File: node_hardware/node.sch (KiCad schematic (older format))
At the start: 22 parts, among them IC1 bluepill, IC2 Ra-01, IC3 TPS73201, J1 Serial, J2 Sensor1, J3 Sensor2

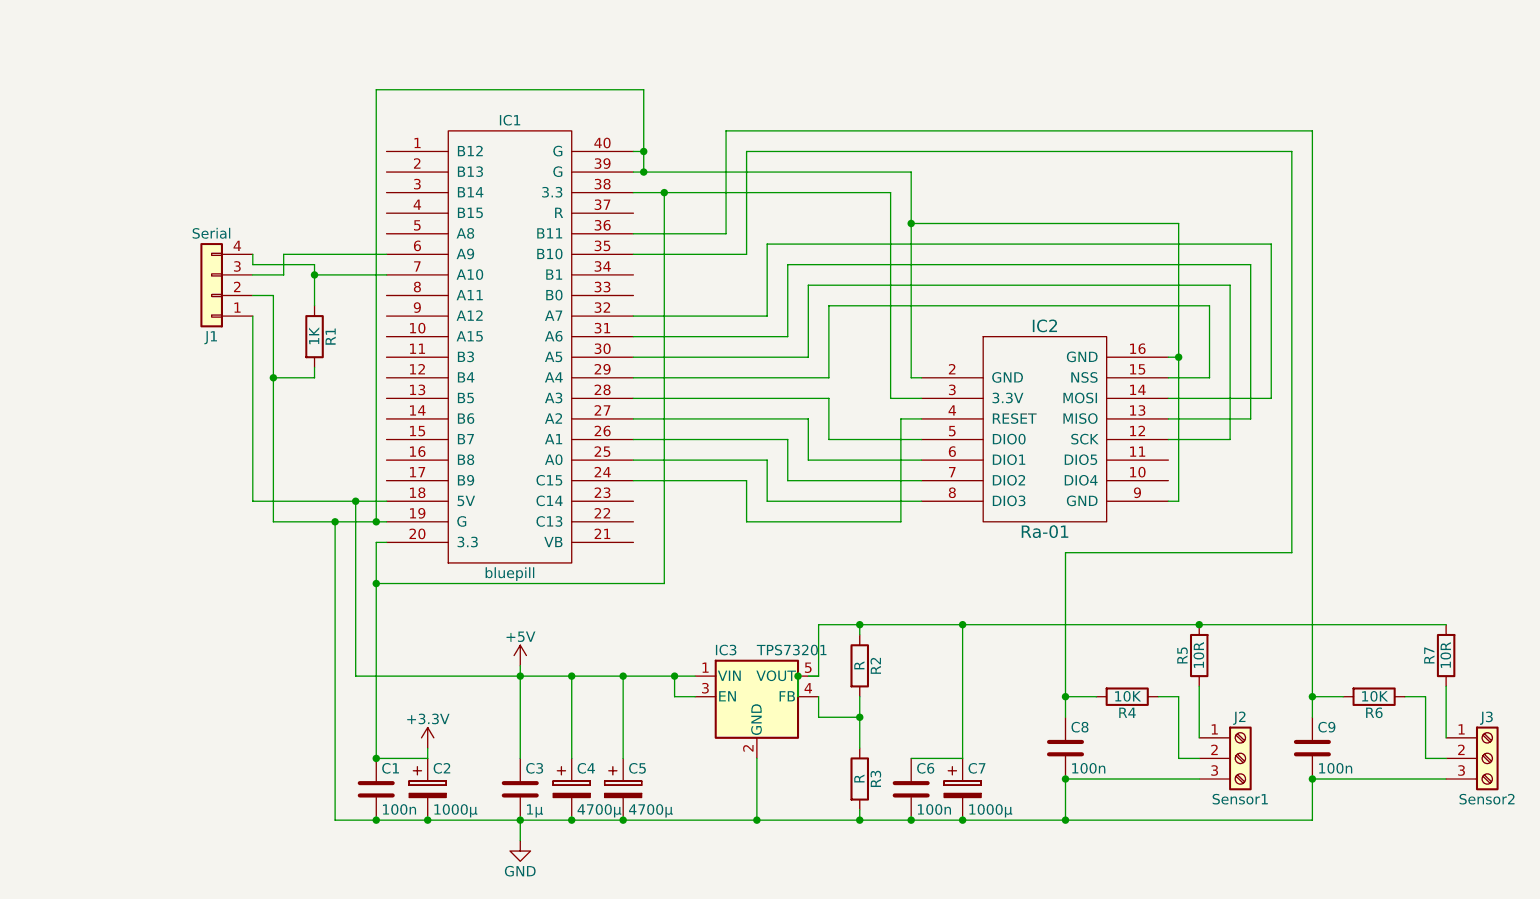
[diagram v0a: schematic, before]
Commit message: Better Layout + added extension headers
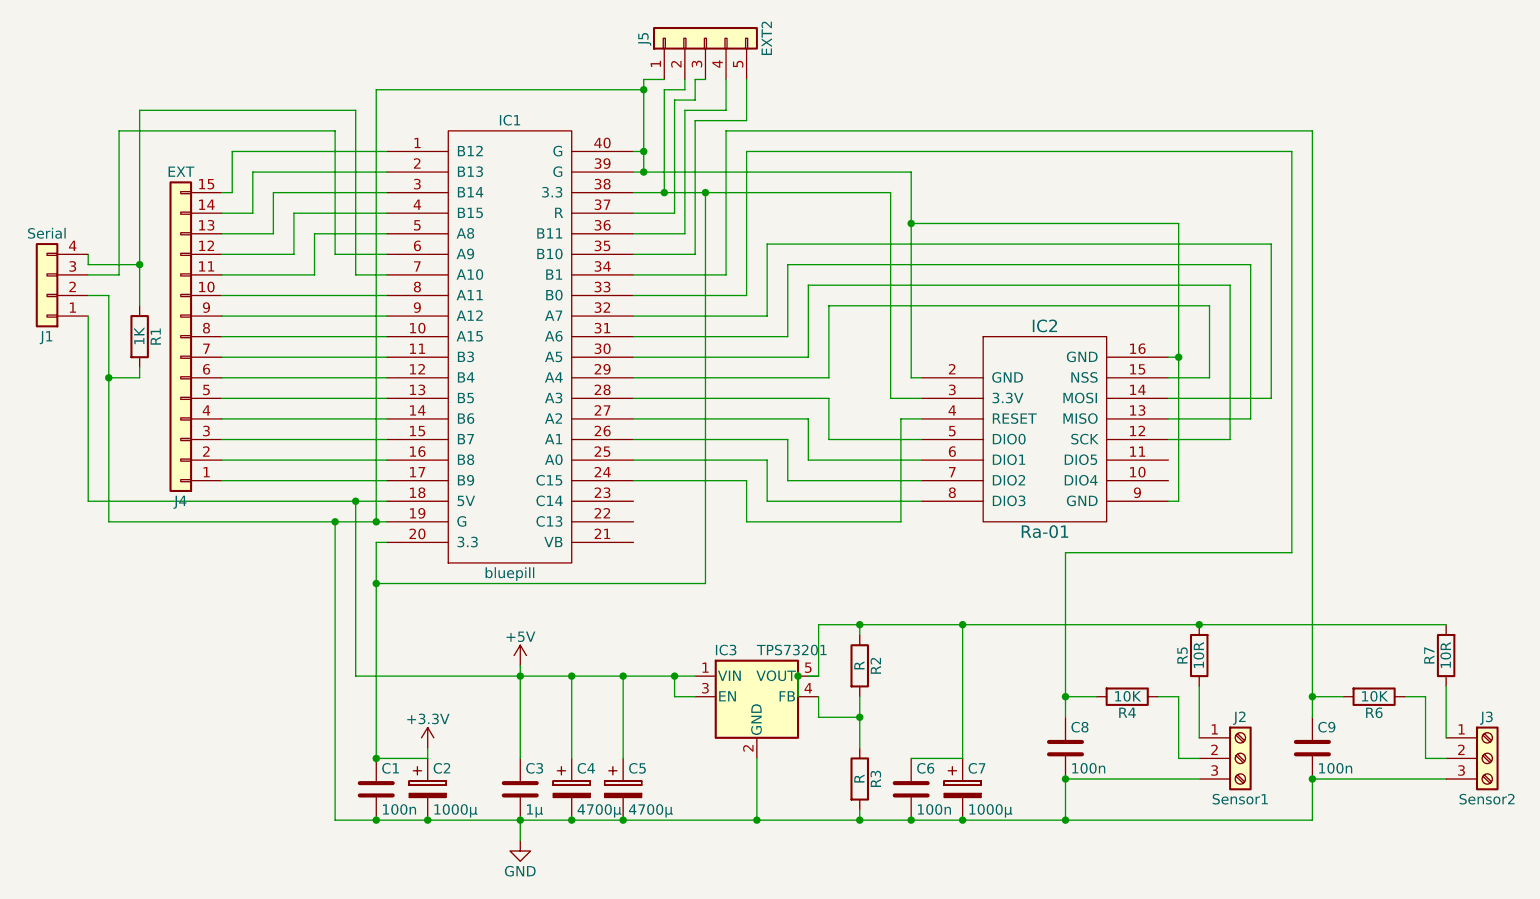
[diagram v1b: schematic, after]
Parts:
- added J4: EXT, Pin_Headers:Pin_Header_Straight_1x15_Pitch2.54mm, symbol Conn_01x15
- added J5: EXT2, Pin_Headers:Pin_Header_Straight_1x05_Pitch2.54mm, symbol Conn_01x05
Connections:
- net +3V3: now also J5.2 (Pin_2)
- net GND: now also J5.1 (Pin_1)
- net at IC1.1 (B12): now also J4.15 (Pin_15)
- net at IC1.10 (A15): now also J4.8 (Pin_8)
- net at IC1.11 (B3): now also J4.7 (Pin_7)
- net at IC1.12 (B4): now also J4.6 (Pin_6)
- net at IC1.13 (B5): now also J4.5 (Pin_5)
- net at IC1.14 (B6): now also J4.4 (Pin_4)
- net at IC1.15 (B7): now also J4.3 (Pin_3)
- net at IC1.16 (B8): now also J4.2 (Pin_2)
- net at IC1.17 (B9): now also J4.1 (Pin_1)
- net at IC1.2 (B13): now also J4.14 (Pin_14)
- net at IC1.3 (B14): now also J4.13 (Pin_13)
- net at IC1.33 (B0): now also C8.1, R4.2
- net at IC1.34 (B1): now also C9.1, R6.2
- net at IC1.37 (R): now also J5.3 (Pin_3)
- net at IC1.4 (B15): now also J4.12 (Pin_12)
- net at IC1.5 (A8): now also J4.11 (Pin_11)
- net at IC1.8 (A11): now also J4.10 (Pin_10)
- net at IC1.9 (A12): now also J4.9 (Pin_9)
- new net: IC1.35 (B10), J5.5 (Pin_5)
- new net: IC1.36 (B11), J5.4 (Pin_4)
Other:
- moved on the sheet: J1, R1
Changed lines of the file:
@@
 L Conn_01x04 J1
 U 1 1 59EA5273
-P 2400 2950
-F 0 "J1" H 2400 3150 50  0000 C CNN
-F 1 "Serial" H 2400 2650 50  0000 C CNN
-F 2 "Pin_Headers:Pin_Header_Straight_1x04_Pitch2.54mm" H 2400 2950 50  0001 C CNN
-F 3 "" H 2400 2950 50  0001 C CNN
-	1    2400 2950
+P 1600 2950
+F 0 "J1" H 1600 3150 50  0000 C CNN
+F 1 "Serial" H 1600 2650 50  0000 C CNN
+F 2 "Pin_Headers:Pin_Header_Straight_1x04_Pitch2.54mm" H 1600 2950 50  0001 C CNN
+F 3 "" H 1600 2950 50  0001 C CNN
+	1    1600 2950
 	-1   0    0    1
 $EndComp
@@
 L R R1
 U 1 1 59EA56C8
-P 2900 3150
-F 0 "R1" V 2980 3150 50  0000 C CNN
-F 1 "1K" V 2900 3150 50  0000 C CNN
-F 2 "Resistors_ThroughHole:R_Axial_DIN0309_L9.0mm_D3.2mm_P12.70mm_Horizontal" V 2830 3150 50  0001 C CNN
-F 3 "" H 2900 3150 50  0001 C CNN
-	1    2900 3150
+P 2050 3150
+F 0 "R1" V 2130 3150 50  0000 C CNN
+F 1 "1K" V 2050 3150 50  0000 C CNN
+F 2 "Resistors_ThroughHole:R_Axial_DIN0309_L9.0mm_D3.2mm_P12.70mm_Horizontal" V 1980 3150 50  0001 C CNN
+F 3 "" H 2050 3150 50  0001 C CNN
+	1    2050 3150
 	1    0    0    -1
 $EndComp
@@
 	5050 5500 5050 5200
 Wire Wire Line
-	5000 2250 5000 2750
-Wire Wire Line
-	5000 2750 4450 2750
+	5000 2250 5000 2950
 Connection ~ 6550 4900
 Wire Wire Line
-	4900 2150 4900 2650
-Wire Wire Line
-	4900 2650 4450 2650
+	4900 2150 4900 2850
 Connection ~ 7750 4900
 Wire Wire Line
@@
 Connection ~ 4400 4800
 Wire Wire Line
-	2700 2950 2700 4050
-Wire Wire Line
-	2700 2950 2600 2950
-Wire Wire Line
-	2600 3050 2600 3950
-Wire Wire Line
-	2900 3300 2900 3350
-Wire Wire Line
-	2900 3350 2700 3350
-Connection ~ 2700 3350
-Wire Wire Line
-	2600 3950 3250 3950
+	1900 2950 1900 4050
+Wire Wire Line
+	1900 2950 1800 2950
+Wire Wire Line
+	1800 3050 1800 3950
+Wire Wire Line
+	2050 3300 2050 3350
+Wire Wire Line
+	2050 3350 1900 3350
+Connection ~ 1900 3350
+Wire Wire Line
+	1800 3950 3250 3950
 Wire Wire Line
 	3100 4800 3100 3950
@@
 Connection ~ 3900 4800
 Wire Wire Line
-	3000 5500 3000 4050
+	3000 4050 3000 5500
 Connection ~ 3000 4050
 Connection ~ 3900 5500
@@
 	3200 4150 3200 5200
 Wire Wire Line
-	2700 4050 3250 4050
+	1900 4050 3250 4050
 Wire Wire Line
 	3200 4150 3250 4150
@@
 	3900 5500 3900 5600
 Wire Wire Line
-	4500 1950 4500 2350
+	4500 1900 4500 2350
 Wire Wire Line
 	4500 2250 4450 2250
@@
 Connection ~ 4500 2250
 Wire Wire Line
-	4600 2450 4600 4350
-Wire Wire Line
-	4600 4350 3200 4350
+	4800 2450 4800 4350
+Wire Wire Line
+	4800 4350 3200 4350
 Connection ~ 3200 4350
-Connection ~ 4600 2450
+Connection ~ 4800 2450
 Wire Wire Line
 	3000 5500 7750 5500
@@
 	6550 4200 7650 4200
 Wire Wire Line
-	3250 2750 2750 2750
-Wire Wire Line
-	2750 2750 2750 2850
-Wire Wire Line
-	2750 2850 2600 2850
-Wire Wire Line
-	2900 3000 2900 2800
-Wire Wire Line
-	2900 2800 2600 2800
-Wire Wire Line
-	2600 2800 2600 2750
-Wire Wire Line
-	3250 2850 2900 2850
-Connection ~ 2900 2850
+	1950 2150 1950 2850
+Wire Wire Line
+	1950 2850 1800 2850
+Wire Wire Line
+	2050 2050 2050 3000
+Wire Wire Line
+	2050 2800 1800 2800
+Wire Wire Line
+	1800 2800 1800 2750
+Wire Wire Line
+	5000 2950 4450 2950
+Wire Wire Line
+	4900 2850 4450 2850
+$Comp
+L Conn_01x15 J4
+U 1 1 59F0A7BB
+P 2250 3150
+F 0 "J4" H 2250 3950 50  0000 C CNN
+F 1 "EXT" H 2250 2350 50  0000 C CNN
+F 2 "Pin_Headers:Pin_Header_Straight_1x15_Pitch2.54mm" H 2250 3150 50  0001 C CNN
+F 3 "" H 2250 3150 50  0001 C CNN
+	1    2250 3150
+	-1   0    0    1
+$EndComp
+Wire Wire Line
+	2450 3850 3250 3850
+Wire Wire Line
+	2450 3750 3250 3750
+Wire Wire Line
+	3250 3650 2450 3650
+Wire Wire Line
+	2450 3550 3250 3550
+Wire Wire Line
+	3250 3450 2450 3450
+Wire Wire Line
+	2450 3350 3250 3350
+Wire Wire Line
+	3250 3250 2450 3250
+Wire Wire Line
+	2450 3150 3250 3150
+Wire Wire Line
+	3250 3050 2450 3050
+Wire Wire Line
+	2450 2950 3250 2950
+Wire Wire Line
+	2450 2450 2500 2450
+Wire Wire Line
+	2500 2450 2500 2250
+Wire Wire Line
+	2500 2250 3250 2250
+Wire Wire Line
+	3250 2350 2600 2350
+Wire Wire Line
+	2600 2350 2600 2550
+Wire Wire Line
+	2600 2550 2450 2550
+Wire Wire Line
+	2450 2650 2700 2650
+Wire Wire Line
+	2700 2650 2700 2450
+Wire Wire Line
+	2700 2450 3250 2450
+Wire Wire Line
+	3250 2550 2800 2550
+Wire Wire Line
+	2800 2550 2800 2750
+Wire Wire Line
+	2800 2750 2450 2750
+Wire Wire Line
+	2450 2850 2900 2850
+Wire Wire Line
+	2900 2850 2900 2650
+Wire Wire Line
+	2900 2650 3250 2650
+Wire Wire Line
+	1950 2150 3000 2150
+Wire Wire Line
+	3000 2150 3000 2750
+Wire Wire Line
+	3000 2750 3250 2750
+Wire Wire Line
+	2050 2050 3100 2050
+Wire Wire Line
+	3100 2050 3100 2850
+Wire Wire Line
+	3100 2850 3250 2850
+Connection ~ 2050 2800
+Wire Wire Line
+	4450 2550 4650 2550
+Wire Wire Line
+	4450 2750 4750 2750
+$Comp
+L Conn_01x05 J5
+U 1 1 59F0D84C
+P 4800 1700
+F 0 "J5" H 4800 2000 50  0000 C CNN
+F 1 "EXT2" H 4800 1400 50  0000 C CNN
+F 2 "Pin_Headers:Pin_Header_Straight_1x05_Pitch2.54mm" H 4800 1700 50  0001 C CNN
+F 3 "" H 4800 1700 50  0001 C CNN
+	1    4800 1700
+	0    -1   -1   0
+$EndComp
+Wire Wire Line
+	4600 1900 4500 1900
+Connection ~ 4500 1950
+Wire Wire Line
+	4700 1900 4700 1950
+Wire Wire Line
+	4700 1950 4600 1950
+Wire Wire Line
+	4600 1950 4600 2450
+Connection ~ 4600 2450
+Wire Wire Line
+	4800 1900 4750 1900
+Wire Wire Line
+	4750 1900 4750 2000
+Wire Wire Line
+	4750 2000 4650 2000
+Wire Wire Line
+	4650 2000 4650 2550
+Wire Wire Line
+	4450 2650 4700 2650
+Wire Wire Line
+	4700 2650 4700 2050
+Wire Wire Line
+	4700 2050 4900 2050
+Wire Wire Line
+	4900 2050 4900 1900
+Wire Wire Line
+	5000 1900 5000 2100
+Wire Wire Line
+	5000 2100 4750 2100
+Wire Wire Line
+	4750 2100 4750 2750
 $EndSCHEMATC
